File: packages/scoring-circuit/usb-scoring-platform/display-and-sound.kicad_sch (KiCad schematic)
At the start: 29 parts, among them J7 TST-108-02-G-D - HUB75, J8 645004114822 - panel 5V, Q1 BSS138-7-F, Q2 BSS138-7-F, U14 SN74AHCT541PWR, U15 SN74AHCT541PWR

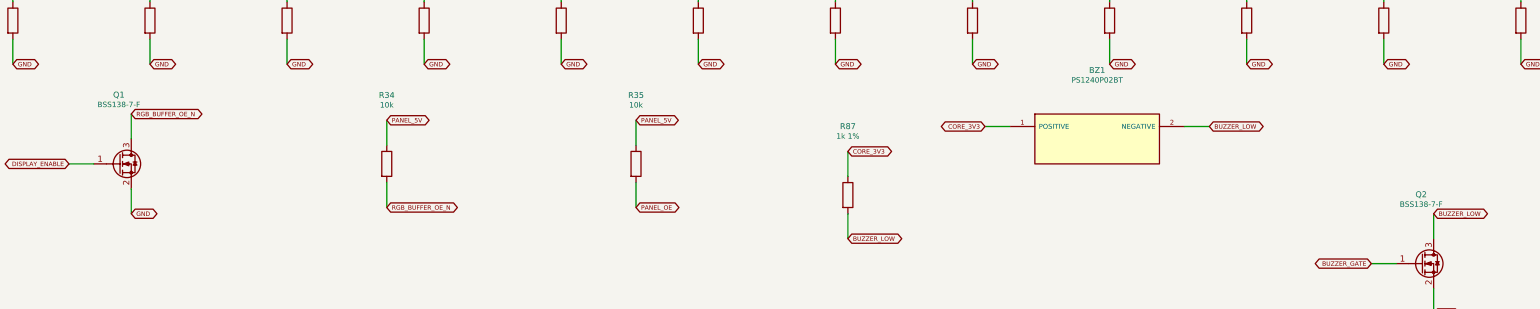
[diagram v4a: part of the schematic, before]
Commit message: fix(scoring-circuit): select low-voltage switching transistors
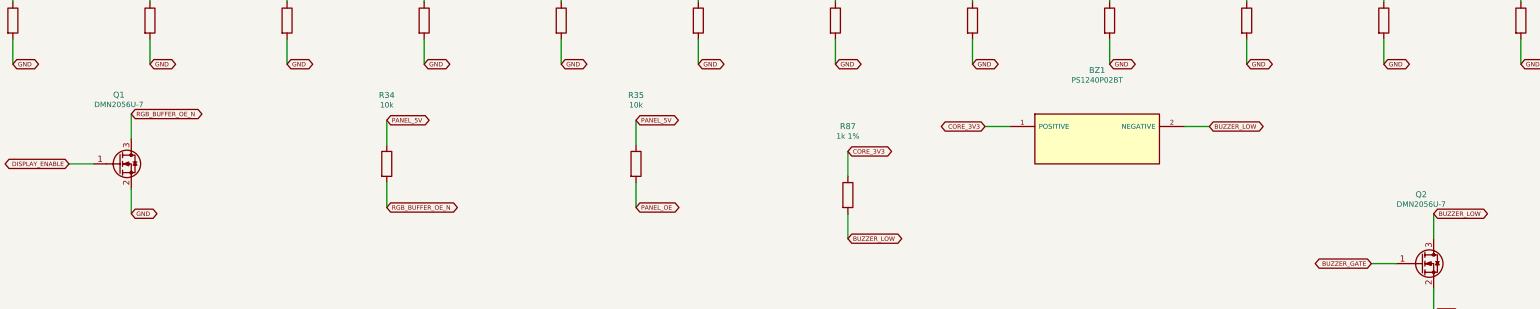
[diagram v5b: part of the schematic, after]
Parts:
- Q1, Q2: value BSS138-7-F -> DMN2056U-7; MPN (none) -> DMN2056U-7; Manufacturer (none) -> Diodes Incorporated
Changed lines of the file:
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@@
 (wire (pts (xy 335.28 149.86) (xy 330.2 149.86)) (stroke (width 0) (type default)))
 (global_label "GND" (shape bidirectional) (at 330.2 149.86 180) (effects (font (size 0.9 0.9)) (justify right)) (property "Intersheetrefs" "" (at 330.2 149.86 180) (effects (font (size 1 1)) (hide yes))))
-(symbol (lib_id "Transistor_FET:BSS138") (at 80.01 204.47 0) (unit 1) (in_bom yes) (on_board yes) (dnp no) (property "Reference" "Q1" (at 80.01 190.39 0) (effects (font (size 1.2 1.2)))) (property "Value" "BSS138-7-F" (at 80.01 192.39 0) (effects (font (size 1.1 1.1)))) (property "Footprint" "Package_TO_SOT_SMD:SOT-23" (at 80.01 204.47 0) (effects (font (size 1 1)) (hide yes))) (pin "1") (pin "2") (pin "3") (instances (project "usb-scoring-platform" (path "/20cc8167-128c-446a-a106-f942323e143f/8eb01a97-00e8-4fc9-a0dc-2c04f64b61fc" (reference "Q1") (unit 1)))))
+(symbol (lib_id "Transistor_FET:BSS138") (at 80.01 204.47 0) (unit 1) (in_bom yes) (on_board yes) (dnp no) (property "Reference" "Q1" (at 80.01 190.39 0) (effects (font (size 1.2 1.2)))) (property "Value" "DMN2056U-7" (at 80.01 192.39 0) (effects (font (size 1.1 1.1)))) (property "Footprint" "Package_TO_SOT_SMD:SOT-23" (at 80.01 204.47 0) (effects (font (size 1 1)) (hide yes))) (pin "1") (pin "2") (pin "3") (instances (project "usb-scoring-platform" (path "/20cc8167-128c-446a-a106-f942323e143f/8eb01a97-00e8-4fc9-a0dc-2c04f64b61fc" (reference "Q1") (unit 1)))) (property "Manufacturer" "Diodes Incorporated" (at 0 0 0) (effects (font (size 1 1)) (hide yes))) (property "MPN" "DMN2056U-7" (at 0 0 0) (effects (font (size 1 1)) (hide yes))) (property "Datasheet" "https://www.diodes.com/datasheet/download/DMN2056U.pdf" (at 0 0 0) (effects (font (size 1 1)) (hide yes))))
 (wire (pts (xy 74.93 204.47) (xy 69.85 204.47)) (stroke (width 0) (type default)))
 (global_label "DISPLAY_ENABLE" (shape bidirectional) (at 69.85 204.47 180) (effects (font (size 0.9 0.9)) (justify right)) (property "Intersheetrefs" "" (at 69.85 204.47 180) (effects (font (size 1 1)) (hide yes))))
@@
 (wire (pts (xy 297.18 196.85) (xy 302.26 196.85)) (stroke (width 0) (type default)))
 (global_label "BUZZER_LOW" (shape bidirectional) (at 302.26 196.85 0) (effects (font (size 0.9 0.9)) (justify left)) (property "Intersheetrefs" "" (at 302.26 196.85 0) (effects (font (size 1 1)) (hide yes))))
-(symbol (lib_id "Transistor_FET:BSS138") (at 345.44 224.79 0) (unit 1) (in_bom yes) (on_board yes) (dnp no) (property "Reference" "Q2" (at 345.44 210.71 0) (effects (font (size 1.2 1.2)))) (property "Value" "BSS138-7-F" (at 345.44 212.71 0) (effects (font (size 1.1 1.1)))) (property "Footprint" "Package_TO_SOT_SMD:SOT-23" (at 345.44 224.79 0) (effects (font (size 1 1)) (hide yes))) (pin "1") (pin "2") (pin "3") (instances (project "usb-scoring-platform" (path "/20cc8167-128c-446a-a106-f942323e143f/8eb01a97-00e8-4fc9-a0dc-2c04f64b61fc" (reference "Q2") (unit 1)))))
+(symbol (lib_id "Transistor_FET:BSS138") (at 345.44 224.79 0) (unit 1) (in_bom yes) (on_board yes) (dnp no) (property "Reference" "Q2" (at 345.44 210.71 0) (effects (font (size 1.2 1.2)))) (property "Value" "DMN2056U-7" (at 345.44 212.71 0) (effects (font (size 1.1 1.1)))) (property "Footprint" "Package_TO_SOT_SMD:SOT-23" (at 345.44 224.79 0) (effects (font (size 1 1)) (hide yes))) (pin "1") (pin "2") (pin "3") (instances (project "usb-scoring-platform" (path "/20cc8167-128c-446a-a106-f942323e143f/8eb01a97-00e8-4fc9-a0dc-2c04f64b61fc" (reference "Q2") (unit 1)))) (property "Manufacturer" "Diodes Incorporated" (at 0 0 0) (effects (font (size 1 1)) (hide yes))) (property "MPN" "DMN2056U-7" (at 0 0 0) (effects (font (size 1 1)) (hide yes))) (property "Datasheet" "https://www.diodes.com/datasheet/download/DMN2056U.pdf" (at 0 0 0) (effects (font (size 1 1)) (hide yes))))
 (wire (pts (xy 340.36 224.79) (xy 335.28 224.79)) (stroke (width 0) (type default)))
 (global_label "BUZZER_GATE" (shape bidirectional) (at 335.28 224.79 180) (effects (font (size 0.9 0.9)) (justify right)) (property "Intersheetrefs" "" (at 335.28 224.79 180) (effects (font (size 1 1)) (hide yes))))

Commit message: chore(scoring-circuit): bind crystal and peripheral ordering details
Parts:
- BZ1: MPN (none) -> PS1240P02BT; Manufacturer (none) -> TDK
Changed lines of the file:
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@@
 (wire (pts (xy 185.42 208.28) (xy 185.42 213.36)) (stroke (width 0) (type default)))
 (global_label "PANEL_OE" (shape bidirectional) (at 185.42 213.36 0) (effects (font (size 0.9 0.9)) (justify left)) (property "Intersheetrefs" "" (at 185.42 213.36 0) (effects (font (size 1 1)) (hide yes))))
-(symbol (lib_id "ScoringPlatform:PS1240P02BT") (at 279.4 199.39 0) (unit 1) (in_bom yes) (on_board yes) (dnp no) (property "Reference" "BZ1" (at 279.4 185.39 0) (effects (font (size 1.2 1.2)))) (property "Value" "PS1240P02BT" (at 279.4 187.39 0) (effects (font (size 1.1 1.1)))) (property "Footprint" "ScoringPlatform:PS1240P02BT" (at 279.4 199.39 0) (effects (font (size 1 1)) (hide yes))) (pin "1") (pin "2") (instances (project "usb-scoring-platform" (path "/20cc8167-128c-446a-a106-f942323e143f/8eb01a97-00e8-4fc9-a0dc-2c04f64b61fc" (reference "BZ1") (unit 1)))))
+(symbol (lib_id "ScoringPlatform:PS1240P02BT") (at 279.4 199.39 0) (unit 1) (in_bom yes) (on_board yes) (dnp no) (property "Reference" "BZ1" (at 279.4 185.39 0) (effects (font (size 1.2 1.2)))) (property "Value" "PS1240P02BT" (at 279.4 187.39 0) (effects (font (size 1.1 1.1)))) (property "Footprint" "ScoringPlatform:PS1240P02BT" (at 279.4 199.39 0) (effects (font (size 1 1)) (hide yes))) (pin "1") (pin "2") (instances (project "usb-scoring-platform" (path "/20cc8167-128c-446a-a106-f942323e143f/8eb01a97-00e8-4fc9-a0dc-2c04f64b61fc" (reference "BZ1") (unit 1)))) (property "Manufacturer" "TDK" (at 0 0 0) (effects (font (size 1 1)) (hide yes))) (property "MPN" "PS1240P02BT" (at 0 0 0) (effects (font (size 1 1)) (hide yes))) (property "Datasheet" "https://product.tdk.com/info/en/catalog/datasheets/piezoelectronic_buzzer_ps_en.pdf" (at 0 0 0) (effects (font (size 1 1)) (hide yes))))
 (wire (pts (xy 261.62 196.85) (xy 256.54 196.85)) (stroke (width 0) (type default)))
 (global_label "CORE_3V3" (shape bidirectional) (at 256.54 196.85 180) (effects (font (size 0.9 0.9)) (justify right)) (property "Intersheetrefs" "" (at 256.54 196.85 180) (effects (font (size 1 1)) (hide yes))))

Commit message: chore(scoring-circuit): complete assembly BOM ordering fields
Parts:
- J7: MPN (none) -> TST-108-02-G-D; Manufacturer (none) -> Samtec
- J8: MPN (none) -> 645004114822; Manufacturer (none) -> Würth Elektronik
- U14, U15: MPN (none) -> SN74AHCT541PWR; Manufacturer (none) -> Texas Instruments
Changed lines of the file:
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@@
 (paper "A3")
 (title_block (title "64x32 HUB75 and scoring sound") (rev "Engineering draft") (comment 1 "NOT FOR FABRICATION"))
-(symbol (lib_id "ScoringPlatform:SN74AHCT541PWR") (at 80.01 90.17 0) (unit 1) (in_bom yes) (on_board yes) (dnp no) (property "Reference" "U14" (at 80.01 69.74 0) (effects (font (size 1.2 1.2)))) (property "Value" "SN74AHCT541PWR" (at 80.01 71.74 0) (effects (font (size 1.1 1.1)))) (property "Footprint" "Package_SO:TSSOP-20_4.4x6.5mm_P0.65mm" (at 80.01 90.17 0) (effects (font (size 1 1)) (hide yes))) (pin "1") (pin "2") (pin "3") (pin "4") (pin "5") (pin "6") (pin "7") (pin "8") (pin "9") (pin "10") (pin "11") (pin "12") (pin "13") (pin "14") (pin "15") (pin "16") (pin "17") (pin "18") (pin "19") (pin "20") (instances (project "usb-scoring-platform" (path "/20cc8167-128c-446a-a106-f942323e143f/8eb01a97-00e8-4fc9-a0dc-2c04f64b61fc" (reference "U14") (unit 1)))))
+(symbol (lib_id "ScoringPlatform:SN74AHCT541PWR") (at 80.01 90.17 0) (unit 1) (in_bom yes) (on_board yes) (dnp no) (property "Reference" "U14" (at 80.01 69.74 0) (effects (font (size 1.2 1.2)))) (property "Value" "SN74AHCT541PWR" (at 80.01 71.74 0) (effects (font (size 1.1 1.1)))) (property "Footprint" "Package_SO:TSSOP-20_4.4x6.5mm_P0.65mm" (at 80.01 90.17 0) (effects (font (size 1 1)) (hide yes))) (pin "1") (pin "2") (pin "3") (pin "4") (pin "5") (pin "6") (pin "7") (pin "8") (pin "9") (pin "10") (pin "11") (pin "12") (pin "13") (pin "14") (pin "15") (pin "16") (pin "17") (pin "18") (pin "19") (pin "20") (instances (project "usb-scoring-platform" (path "/20cc8167-128c-446a-a106-f942323e143f/8eb01a97-00e8-4fc9-a0dc-2c04f64b61fc" (reference "U14") (unit 1)))) (property "Manufacturer" "Texas Instruments" (at 0 0 0) (effects (font (size 1 1)) (hide yes))) (property "MPN" "SN74AHCT541PWR" (at 0 0 0) (effects (font (size 1 1)) (hide yes))))
 (wire (pts (xy 62.23 78.74) (xy 57.15 78.74)) (stroke (width 0) (type default)))
 (global_label "GND" (shape bidirectional) (at 57.15 78.74 180) (effects (font (size 0.9 0.9)) (justify right)) (property "Intersheetrefs" "" (at 57.15 78.74 180) (effects (font (size 1 1)) (hide yes))))
@@
 (wire (pts (xy 74.93 148.59) (xy 74.93 153.67)) (stroke (width 0) (type default)))
 (global_label "GND" (shape bidirectional) (at 74.93 153.67 0) (effects (font (size 0.9 0.9)) (justify left)) (property "Intersheetrefs" "" (at 74.93 153.67 0) (effects (font (size 1 1)) (hide yes))))
-(symbol (lib_id "ScoringPlatform:SN74AHCT541PWR") (at 214.63 90.17 0) (unit 1) (in_bom yes) (on_board yes) (dnp no) (property "Reference" "U15" (at 214.63 69.74 0) (effects (font (size 1.2 1.2)))) (property "Value" "SN74AHCT541PWR" (at 214.63 71.74 0) (effects (font (size 1.1 1.1)))) (property "Footprint" "Package_SO:TSSOP-20_4.4x6.5mm_P0.65mm" (at 214.63 90.17 0) (effects (font (size 1 1)) (hide yes))) (pin "1") (pin "2") (pin "3") (pin "4") (pin "5") (pin "6") (pin "7") (pin "8") (pin "9") (pin "10") (pin "11") (pin "12") (pin "13") (pin "14") (pin "15") (pin "16") (pin "17") (pin "18") (pin "19") (pin "20") (instances (project "usb-scoring-platform" (path "/20cc8167-128c-446a-a106-f942323e143f/8eb01a97-00e8-4fc9-a0dc-2c04f64b61fc" (reference "U15") (unit 1)))))
+(symbol (lib_id "ScoringPlatform:SN74AHCT541PWR") (at 214.63 90.17 0) (unit 1) (in_bom yes) (on_board yes) (dnp no) (property "Reference" "U15" (at 214.63 69.74 0) (effects (font (size 1.2 1.2)))) (property "Value" "SN74AHCT541PWR" (at 214.63 71.74 0) (effects (font (size 1.1 1.1)))) (property "Footprint" "Package_SO:TSSOP-20_4.4x6.5mm_P0.65mm" (at 214.63 90.17 0) (effects (font (size 1 1)) (hide yes))) (pin "1") (pin "2") (pin "3") (pin "4") (pin "5") (pin "6") (pin "7") (pin "8") (pin "9") (pin "10") (pin "11") (pin "12") (pin "13") (pin "14") (pin "15") (pin "16") (pin "17") (pin "18") (pin "19") (pin "20") (instances (project "usb-scoring-platform" (path "/20cc8167-128c-446a-a106-f942323e143f/8eb01a97-00e8-4fc9-a0dc-2c04f64b61fc" (reference "U15") (unit 1)))) (property "Manufacturer" "Texas Instruments" (at 0 0 0) (effects (font (size 1 1)) (hide yes))) (property "MPN" "SN74AHCT541PWR" (at 0 0 0) (effects (font (size 1 1)) (hide yes))))
 (wire (pts (xy 196.85 78.74) (xy 191.77 78.74)) (stroke (width 0) (type default)))
 (global_label "GND" (shape bidirectional) (at 191.77 78.74 180) (effects (font (size 0.9 0.9)) (justify right)) (property "Intersheetrefs" "" (at 191.77 78.74 180) (effects (font (size 1 1)) (hide yes))))
@@
 (wire (pts (xy 209.55 148.59) (xy 209.55 153.67)) (stroke (width 0) (type default)))
 (global_label "GND" (shape bidirectional) (at 209.55 153.67 0) (effects (font (size 0.9 0.9)) (justify left)) (property "Intersheetrefs" "" (at 209.55 153.67 0) (effects (font (size 1 1)) (hide yes))))
-(symbol (lib_id "Connector_Generic:Conn_02x08_Odd_Even") (at 340.36 80.01 0) (unit 1) (in_bom yes) (on_board yes) (dnp no) (property "Reference" "J7" (at 340.36 63.39 0) (effects (font (size 1.2 1.2)))) (property "Value" "TST-108-02-G-D - HUB75" (at 340.36 65.39 0) (effects (font (size 1.1 1.1)))) (property "Footprint" "ScoringPlatform:HUB75" (at 340.36 80.01 0) (effects (font (size 1 1)) (hide yes))) (pin "1") (pin "2") (pin "3") (pin "4") (pin "5") (pin "6") (pin "7") (pin "8") (pin "9") (pin "10") (pin "11") (pin "12") (pin "13") (pin "14") (pin "15") (pin "16") (instances (project "usb-scoring-platform" (path "/20cc8167-128c-446a-a106-f942323e143f/8eb01a97-00e8-4fc9-a0dc-2c04f64b61fc" (reference "J7") (unit 1)))))
+(symbol (lib_id "Connector_Generic:Conn_02x08_Odd_Even") (at 340.36 80.01 0) (unit 1) (in_bom yes) (on_board yes) (dnp no) (property "Reference" "J7" (at 340.36 63.39 0) (effects (font (size 1.2 1.2)))) (property "Value" "TST-108-02-G-D - HUB75" (at 340.36 65.39 0) (effects (font (size 1.1 1.1)))) (property "Footprint" "ScoringPlatform:HUB75" (at 340.36 80.01 0) (effects (font (size 1 1)) (hide yes))) (pin "1") (pin "2") (pin "3") (pin "4") (pin "5") (pin "6") (pin "7") (pin "8") (pin "9") (pin "10") (pin "11") (pin "12") (pin "13") (pin "14") (pin "15") (pin "16") (instances (project "usb-scoring-platform" (path "/20cc8167-128c-446a-a106-f942323e143f/8eb01a97-00e8-4fc9-a0dc-2c04f64b61fc" (reference "J7") (unit 1)))) (property "Manufacturer" "Samtec" (at 0 0 0) (effects (font (size 1 1)) (hide yes))) (property "MPN" "TST-108-02-G-D" (at 0 0 0) (effects (font (size 1 1)) (hide yes))))
 (wire (pts (xy 335.28 72.39) (xy 330.2 72.39)) (stroke (width 0) (type default)))
 (global_label "PANEL_R1" (shape bidirectional) (at 330.2 72.39 180) (effects (font (size 0.9 0.9)) (justify right)) (property "Intersheetrefs" "" (at 330.2 72.39 180) (effects (font (size 1 1)) (hide yes))))
@@
 (wire (pts (xy 347.98 90.17) (xy 353.06 90.17)) (stroke (width 0) (type default)))
 (global_label "GND" (shape bidirectional) (at 353.06 90.17 0) (effects (font (size 0.9 0.9)) (justify left)) (property "Intersheetrefs" "" (at 353.06 90.17 0) (effects (font (size 1 1)) (hide yes))))
-(symbol (lib_id "Connector_Generic:Conn_01x04") (at 340.36 144.78 0) (unit 1) (in_bom yes) (on_board yes) (dnp no) (property "Reference" "J8" (at 340.36 130.78 0) (effects (font (size 1.2 1.2)))) (property "Value" "645004114822 - panel 5V" (at 340.36 132.78 0) (effects (font (size 1.1 1.1)))) (property "Footprint" "ScoringPlatform:HUB75_POWER" (at 340.36 144.78 0) (effects (font (size 1 1)) (hide yes))) (pin "1") (pin "2") (pin "3") (pin "4") (instances (project "usb-scoring-platform" (path "/20cc8167-128c-446a-a106-f942323e143f/8eb01a97-00e8-4fc9-a0dc-2c04f64b61fc" (reference "J8") (unit 1)))))
+(symbol (lib_id "Connector_Generic:Conn_01x04") (at 340.36 144.78 0) (unit 1) (in_bom yes) (on_board yes) (dnp no) (property "Reference" "J8" (at 340.36 130.78 0) (effects (font (size 1.2 1.2)))) (property "Value" "645004114822 - panel 5V" (at 340.36 132.78 0) (effects (font (size 1.1 1.1)))) (property "Footprint" "ScoringPlatform:HUB75_POWER" (at 340.36 144.78 0) (effects (font (size 1 1)) (hide yes))) (pin "1") (pin "2") (pin "3") (pin "4") (instances (project "usb-scoring-platform" (path "/20cc8167-128c-446a-a106-f942323e143f/8eb01a97-00e8-4fc9-a0dc-2c04f64b61fc" (reference "J8") (unit 1)))) (property "Manufacturer" "Würth Elektronik" (at 0 0 0) (effects (font (size 1 1)) (hide yes))) (property "MPN" "645004114822" (at 0 0 0) (effects (font (size 1 1)) (hide yes))))
 (wire (pts (xy 335.28 142.24) (xy 330.2 142.24)) (stroke (width 0) (type default)))
 (global_label "PANEL_5V" (shape bidirectional) (at 330.2 142.24 180) (effects (font (size 0.9 0.9)) (justify right)) (property "Intersheetrefs" "" (at 330.2 142.24 180) (effects (font (size 1 1)) (hide yes))))
